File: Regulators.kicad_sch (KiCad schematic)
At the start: 20 parts, among them J5 24V Logic, J6 24V Peripheral

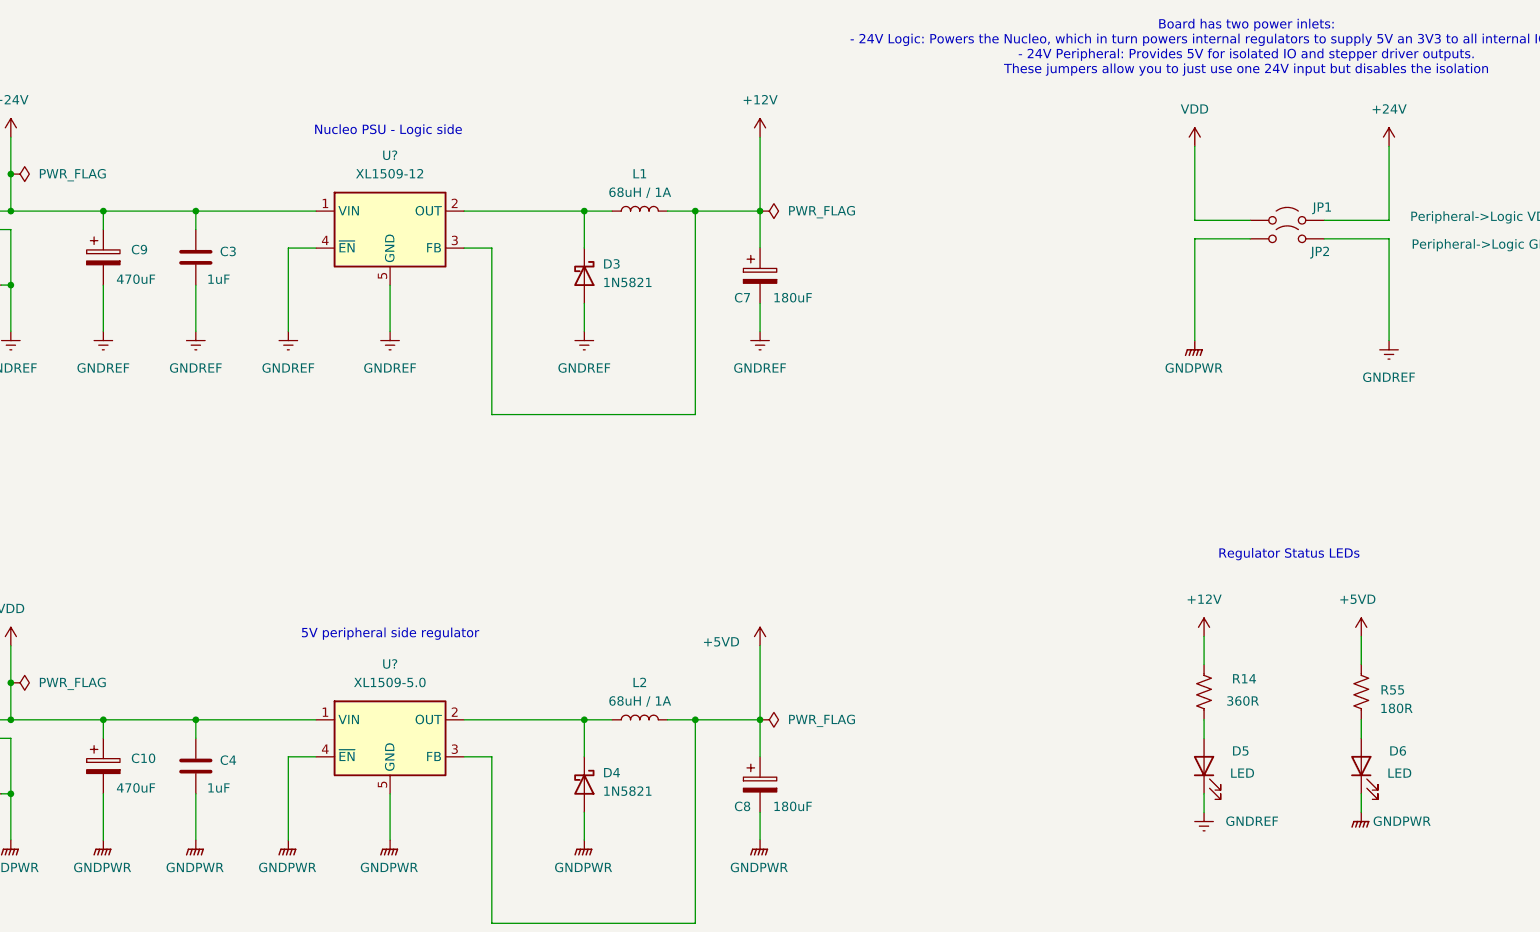
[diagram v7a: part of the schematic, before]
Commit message: New PSU designs + footprints assigned. Changes to board shape to make room for new components. BOM consolidation of supplimentary file
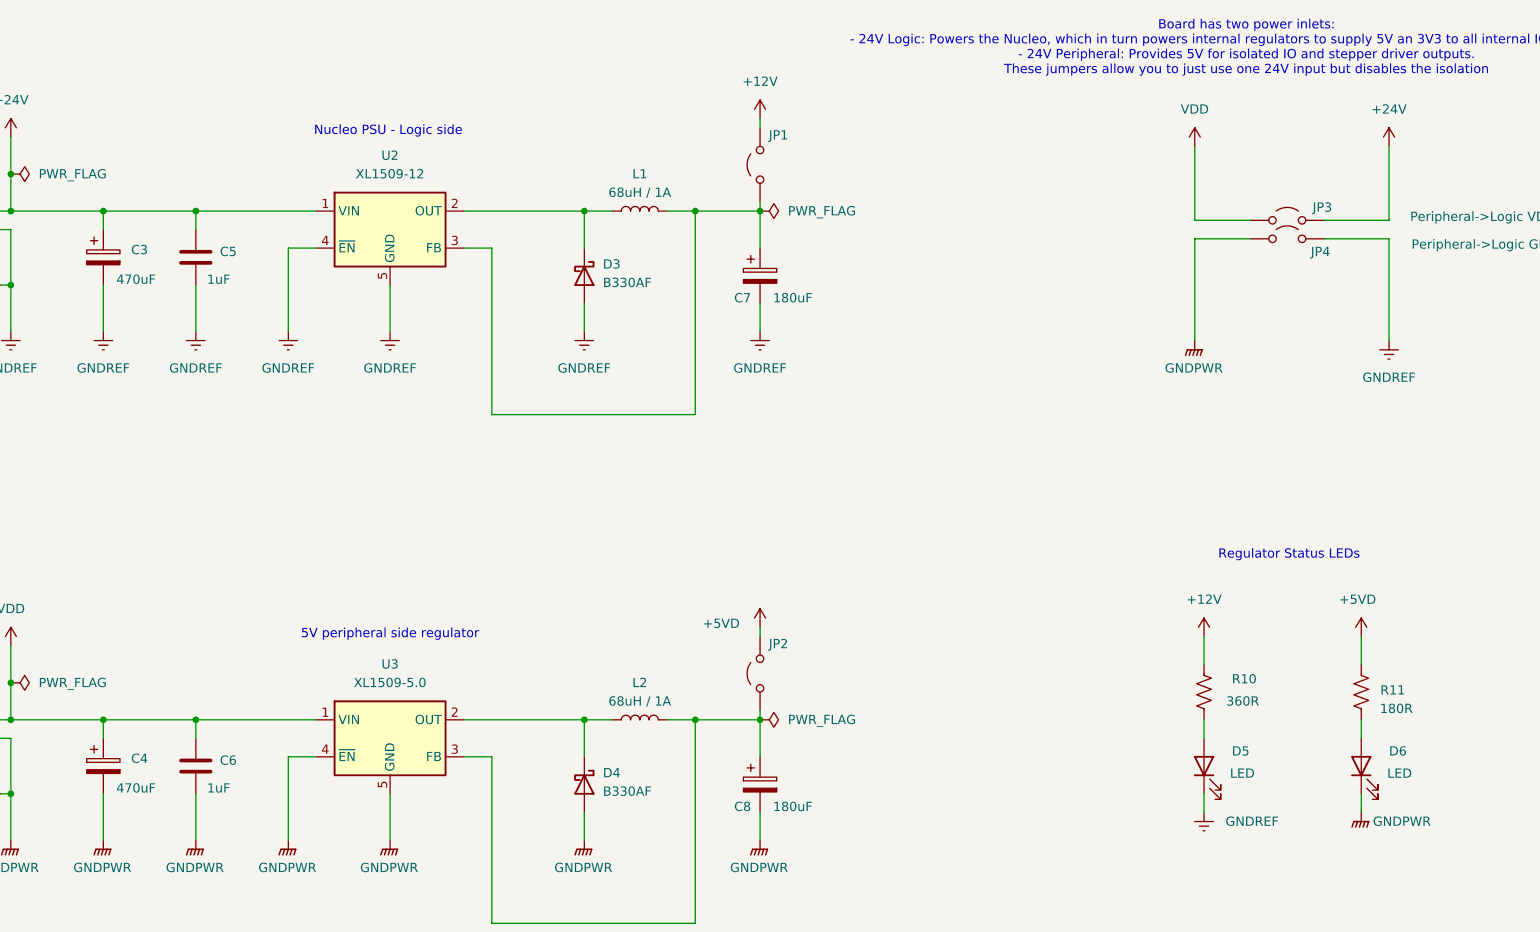
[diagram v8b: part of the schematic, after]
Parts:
- added JP1, JP2: Peripheral->Logic VDD Jumper, Jumper:SolderJumper-2_P1.3mm_Bridged2Bar_RoundedPad1.0x1.5mm, symbol Jumper:Jumper_2_Open
- C3: renamed from C9; footprint (none) -> Capacitor_THT:CP_Radial_D8.0mm_P3.50mm; Digikey Part Number (none) -> 493-12789-1-ND; Digikey URL (none) -> https://www.digikey.com.au/en/products/detail/nichicon/UVR1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
- C4: renamed from C10; footprint (none) -> Capacitor_THT:CP_Radial_D8.0mm_P3.50mm; Digikey Part Number (none) -> 493-12789-1-ND; Digikey URL (none) -> https://www.digikey.com.au/en/products/detail/nichicon/UVR1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
- C5: renamed from C3; footprint (none) -> Capacitor_SMD:C_1206_3216Metric_Pad1.33x1.80mm_HandSolder; Digikey Part Number (none) -> 1276-1068-1-ND; Digikey URL (none) -> https://www.digikey.com.au/en/products/detail/samsung-elect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
- C6: renamed from C4; footprint (none) -> Capacitor_SMD:C_1206_3216Metric_Pad1.33x1.80mm_HandSolder; Digikey Part Number (none) -> 1276-1068-1-ND; Digikey URL (none) -> https://www.digikey.com.au/en/products/detail/samsung-elect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
- C7, C8: footprint (none) -> Capacitor_THT:CP_Radial_D6.3mm_P2.50mm; Digikey Part Number (none) -> 732-8633-1-ND; Digikey URL (none) -> https://www.digikey.com.au/en/products/detail/w%C3%BCrth-el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
- D3, D4: value 1N5821 -> B330AF; footprint Diode_SMD:D_1206_3216Metric_Pad1.42x1.75mm_HandSolder -> Diode_SMD:D_SMA; Digikey Part Number (none) -> B330AF-13DICT-ND; Digikey URL (none) -> https://www.digikey.com.au/en/products/detail/diodes-incorp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
- J5, J6: Digikey Part Number (none) -> 1818-QT02ADP83V0000G-ND; Digikey URL (none) -> https://www.digikey.com.au/en/products/detail/amphenol-anyt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
- JP3: renamed from JP1; now left out of the parts list
- JP4: renamed from JP2; now left out of the parts list
- L1, L2: footprint (none) -> Inductor_SMD:L_APV_ANR8040; Digikey Part Number (none) -> SDE0805A-680KCT-ND; Digikey URL (none) -> https://www.digikey.com.au/en/products/detail/bourns-inc/SD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
- U2: renamed from U?; Digikey Part Number (none) -> 4518-XL1509-12CT-ND; Digikey URL (none) -> https://www.digikey.com.au/en/products/detail/umw/xl1509-12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
- U3: renamed from U?; Digikey Part Number (none) -> 4518-XL1509-5.0CT-ND; Digikey URL (none) -> https://www.digikey.com.au/en/products/detail/umw/XL1509-5-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
- renumbered R14 to R10, R55 to R11
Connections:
- net +12V: now also JP1.2 (B); no longer C7.1, L1.2, U2.3 (FB)
- net +5VD: now also JP2.2 (B); no longer C8.1, L2.2, U3.3 (FB)
- new net: C7.1, JP1.1 (A), L1.2, U2.3 (FB)
- new net: C8.1, JP2.1 (A), L2.2, U3.3 (FB)
